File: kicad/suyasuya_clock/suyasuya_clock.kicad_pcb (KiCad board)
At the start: 2 copper layers, 66 x 78.7 mm, 33 parts, among them J1 Jack-DC, J2 Conn_Writer, J3 Conn_GPS, J4 USB_OUTPUT, Q1 2sk4017, SW1 RESET, U1 ATmega328-P, U2 BA50DD0T, U3 7803, Y1 Ceralock

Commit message: アートワーク修正
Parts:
- moved R1 117.3 mm to (208.3, 119.4)
- moved Y1 117.1 mm to (231.1, 68.6)
- moved C1 115.9 mm to (218.5, 68.6)
- moved R6 114.8 mm to (195.6, 61.0)
- moved R7 114.8 mm to (195.6, 58.4)
- moved SW1 114.8 mm to (205.7, 50.8)
- moved U1 114.8 mm to (205.7, 66.0)
- moved C5 114.8 mm to (205.7, 71.1)
- moved D3 114.8 mm to (228.6, 53.3)
- moved D8 114.8 mm to (215.9, 68.6)
- moved J2 114.8 mm to (200.7, 68.6)
- moved Q1 114.8 mm to (198.1, 61.0)
- moved R2 114.8 mm to (228.6, 50.8)
- moved R3 114.8 mm to (226.1, 53.3)
- moved R5 114.8 mm to (198.1, 48.3)
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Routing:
- net GND: track 253.8 -> 289.6 mm, vias 6 -> 5
- net +5V: track 239.4 -> 266.8 mm
- net +3V3: track 62.0 -> 86.4 mm
- net Net-(D8-Pad2): track 33.0 -> 38.1 mm
- net RX: track 15.2 -> 10.2 mm
- net GPS_RX: track 43.2 -> 48.3 mm
- net Net-(D1-Pad2): track 10.2 -> 7.62 mm
- net +12V: track 55.9 -> 53.5 mm
- net Net-(U1-Pad9): track 3.59 -> 2.54 mm
- net Net-(U1-Pad10): track 2.54 -> 3.59 mm
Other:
- board size 66 x 78.7 mm -> 71.1 x 94 mm

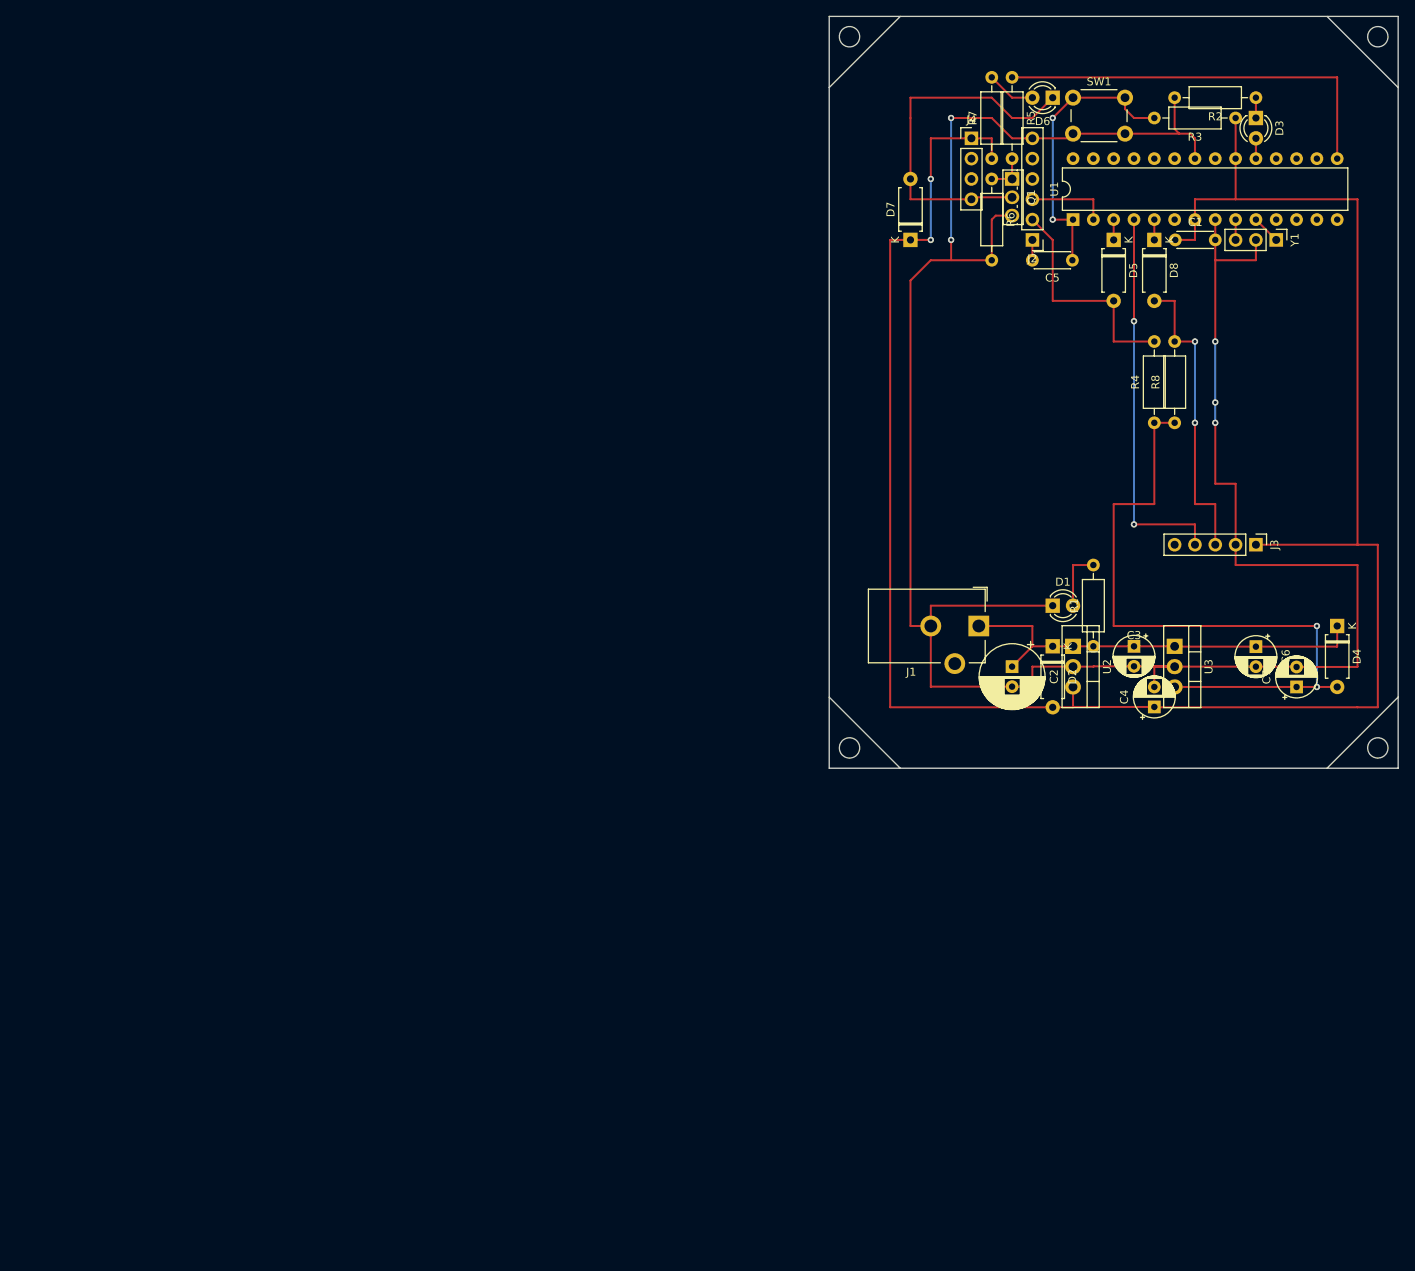
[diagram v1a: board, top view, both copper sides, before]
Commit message: ファーム変更・回路修正
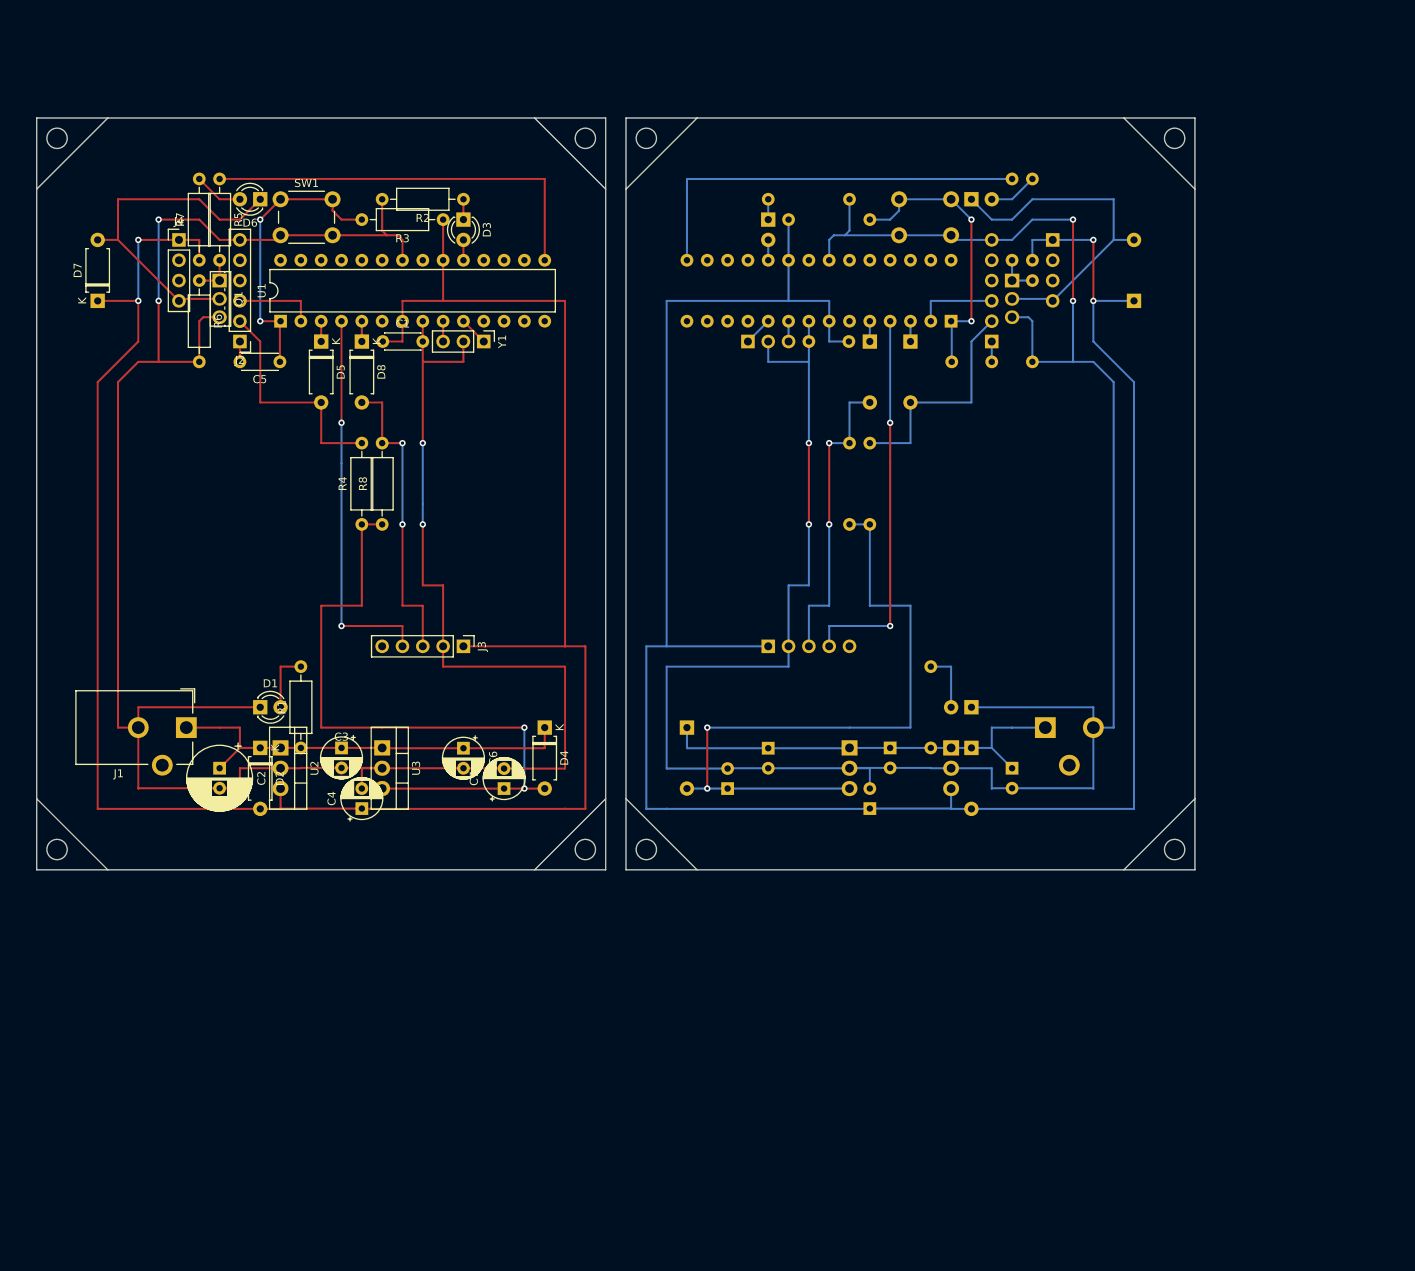
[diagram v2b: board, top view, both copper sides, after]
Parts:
- added C1: 104, Capacitor_THT:C_Disc_D4.3mm_W1.9mm_P5.00mm, B.Cu at (177.7, 81.3)
- added C2: 100u, Capacitor_THT:CP_Radial_D8.0mm_P2.50mm, B.Cu at (198.1, 134.6)
- added C3: 10u, Capacitor_THT:CP_Radial_D5.0mm_P2.50mm, B.Cu at (182.9, 132.1)
- added C4: 22u, Capacitor_THT:CP_Radial_D5.0mm_P2.50mm, B.Cu at (180.3, 139.7)
- added C5: 104, Capacitor_THT:C_Disc_D4.3mm_W1.9mm_P5.00mm, B.Cu at (190.6, 83.8)
- added C6: 10u, Capacitor_THT:CP_Radial_D5.0mm_P2.50mm, B.Cu at (167.6, 132.1)
- added C7: 22u, Capacitor_THT:CP_Radial_D5.0mm_P2.50mm, B.Cu at (162.6, 137.2)
- added D1: LED_12V, LED_THT:LED_D3.0mm, B.Cu at (193.0, 127.0)
- added D2: 1s4, Diode_THT:D_A-405_P7.62mm_Horizontal, B.Cu at (193.0, 132.1)
- added D3: LED, LED_THT:LED_D3.0mm, B.Cu at (167.6, 66.0)
- added D4: 1s4, Diode_THT:D_A-405_P7.62mm_Horizontal, B.Cu at (157.5, 129.5)
- added D5: 1s4, Diode_THT:D_A-405_P7.62mm_Horizontal, B.Cu at (185.4, 81.3)
- added D6: LED, LED_THT:LED_D3.0mm, B.Cu at (193.0, 63.5)
- added D7: 1s4, Diode_THT:D_A-405_P7.62mm_Horizontal, B.Cu at (213.4, 76.2)
- added D8: 1s4, Diode_THT:D_A-405_P7.62mm_Horizontal, B.Cu at (180.3, 81.3)
- added J1: Jack-DC, Connector_BarrelJack:BarrelJack_CUI_PJ-102AH_Horizontal, B.Cu at (202.3, 129.5)
- added J2: Conn_Writer, Connector_PinHeader_2.54mm:PinHeader_1x06_P2.54mm_Vertical, B.Cu at (195.6, 81.3)
- added J3: Conn_GPS, Connector_PinHeader_2.54mm:PinHeader_1x05_P2.54mm_Vertical, B.Cu at (167.6, 119.4)
- added J4: USB_OUTPUT, Connector_PinHeader_2.54mm:PinHeader_1x04_P2.54mm_Vertical, B.Cu at (203.2, 68.6)
- added Q1: 2sk4017, Package_TO_SOT_THT:TO-251-3_Vertical, B.Cu at (198.1, 73.7)
- added R1: 10k, Resistor_THT:R_Axial_DIN0207_L6.3mm_D2.5mm_P10.16mm_Horizontal, B.Cu at (188.0, 132.1)
- added R2: 1k, Resistor_THT:R_Axial_DIN0207_L6.3mm_D2.5mm_P10.16mm_Horizontal, B.Cu at (167.6, 63.5)
- added R3: 10k, Resistor_THT:R_Axial_DIN0207_L6.3mm_D2.5mm_P10.16mm_Horizontal, B.Cu at (170.2, 66.0)
- added R4: 10k, Resistor_THT:R_Axial_DIN0207_L6.3mm_D2.5mm_P10.16mm_Horizontal, B.Cu at (180.3, 104.1)
- added R5: 100, Resistor_THT:R_Axial_DIN0207_L6.3mm_D2.5mm_P10.16mm_Horizontal, B.Cu at (198.1, 61.0)
- added R6: 10k, Resistor_THT:R_Axial_DIN0207_L6.3mm_D2.5mm_P10.16mm_Horizontal, B.Cu at (200.7, 73.7)
- added R7: 1k, Resistor_THT:R_Axial_DIN0207_L6.3mm_D2.5mm_P10.16mm_Horizontal, B.Cu at (200.7, 71.1)
- added R8: 10k, Resistor_THT:R_Axial_DIN0207_L6.3mm_D2.5mm_P10.16mm_Horizontal, B.Cu at (177.8, 104.1)
- added SW1: RESET, Button_Switch_THT:SW_PUSH_6mm, B.Cu at (190.5, 63.5)
- added U1: ATmega328-P, Package_DIP:DIP-28_W7.62mm, B.Cu at (190.5, 78.7)
- added U2: BA50DD0T, Package_TO_SOT_THT:TO-220-3_Vertical, B.Cu at (190.5, 132.1)
- added U3: 7803, Package_TO_SOT_THT:TO-220-3_Vertical, B.Cu at (177.8, 132.1)
- added Y1: Ceralock, Connector_PinHeader_2.54mm:PinHeader_1x03_P2.54mm_Vertical, B.Cu at (165.1, 81.3)
- moved D7 101.9 mm to (83.8, 76.2)
- moved C1 99.9 mm to (119.5, 81.3)
- moved C3 99.9 mm to (114.3, 132.1)
- moved R6 99.9 mm to (96.5, 73.7)
- moved R7 99.9 mm to (96.5, 71.1)
- moved C2 99.9 mm to (99.1, 134.6)
- moved C4 99.9 mm to (116.8, 139.7)
- moved C5 99.9 mm to (106.6, 83.8)
- moved C6 99.9 mm to (129.5, 132.1)
- moved C7 99.9 mm to (134.6, 137.2)
- moved D3 99.9 mm to (129.5, 66.0)
- moved D4 99.9 mm to (139.7, 129.5)
- moved D8 99.9 mm to (116.8, 81.3)
- moved J1 99.9 mm to (94.9, 129.5)
- moved J2 99.9 mm to (101.6, 81.3)
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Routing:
- net GND: track 289.6 -> 579.1 mm, vias 5 -> 8
- net +5V: track 266.8 -> 537.8 mm, vias 2 -> 4
- net +3V3: track 86.4 -> 172.7 mm, vias 2 -> 4
- net +12V: track 53.5 -> 107.0 mm
- net TRIG: track 50.8 -> 101.6 mm
- net GPS_RX: track 48.3 -> 96.5 mm, vias 2 -> 4
- net Net-(D7-Pad2): track 45.4 -> 86.9 mm
- net Net-(D8-Pad2): track 38.1 -> 76.2 mm, vias 2 -> 4
- net Net-(C5-Pad1): track 36.0 -> 72.0 mm, vias 2 -> 4
- net Net-(D5-Pad2): track 29.0 -> 58.0 mm
- net RX: track 10.2 -> 20.3 mm
- net Net-(D1-Pad2): track 7.62 -> 15.2 mm
- net Net-(R7-Pad2): track 6.13 -> 12.3 mm
- net Net-(Q1-Pad1): track 5.08 -> 10.2 mm
- net Net-(U1-Pad10): track 3.59 -> 7.18 mm
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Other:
- board size 71.1 x 94 mm -> 144.8 x 94 mm
